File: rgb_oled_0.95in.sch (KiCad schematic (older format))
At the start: 12 parts, among them J1 PMOD, U1 LMR62014, U2 UG-9664HDDAG01

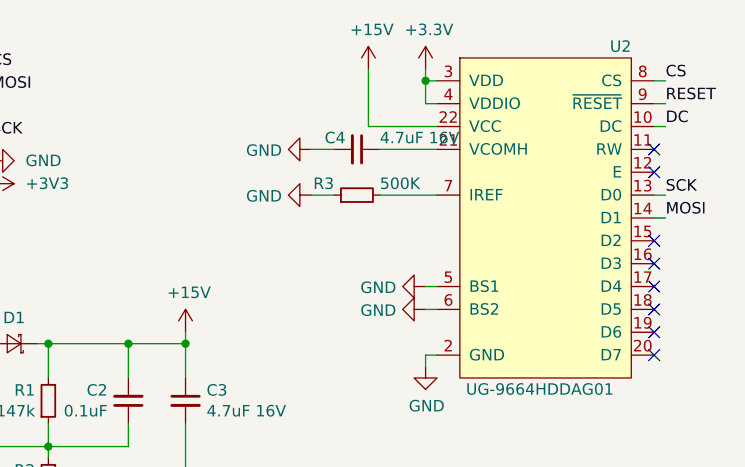
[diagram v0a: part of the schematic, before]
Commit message: Add nicer silk
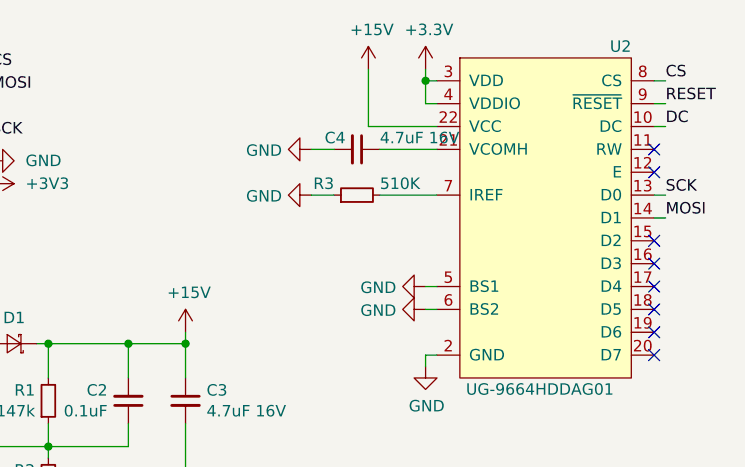
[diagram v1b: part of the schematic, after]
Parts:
- R3: value 500K -> 510K
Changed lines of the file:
@@
 EESchema Schematic File Version 4
+LIBS:rgb_oled_0.95in-cache
 EELAYER 29 0
 EELAYER END
@@
 P 6750 3600
 F 0 "R3" V 6800 3700 50  0000 L CNN
-F 1 "500K" V 6800 3500 50  0000 R CNN
+F 1 "510K" V 6800 3500 50  0000 R CNN
 F 2 "Capacitor_SMD:C_0603_1608Metric" H 6750 3600 50  0001 C CNN
 F 3 "~" H 6750 3600 50  0001 C CNN
